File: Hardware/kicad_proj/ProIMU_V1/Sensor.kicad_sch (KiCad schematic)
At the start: 5 parts

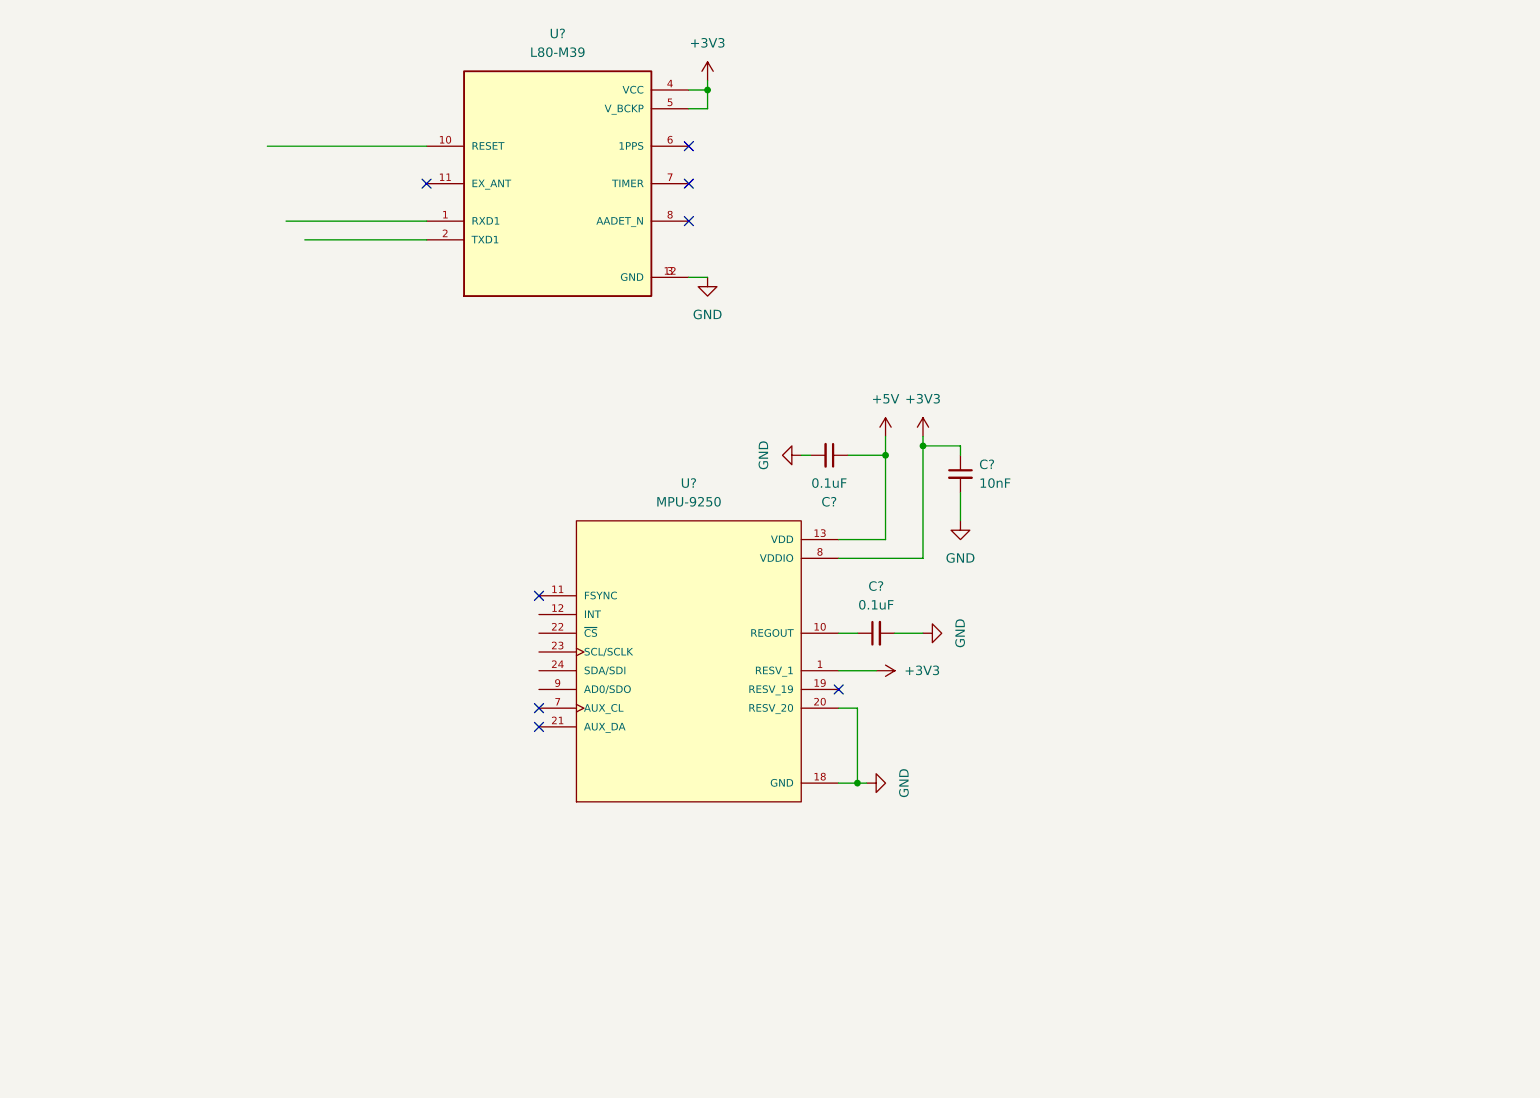
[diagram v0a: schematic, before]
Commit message: Added sensor schematic
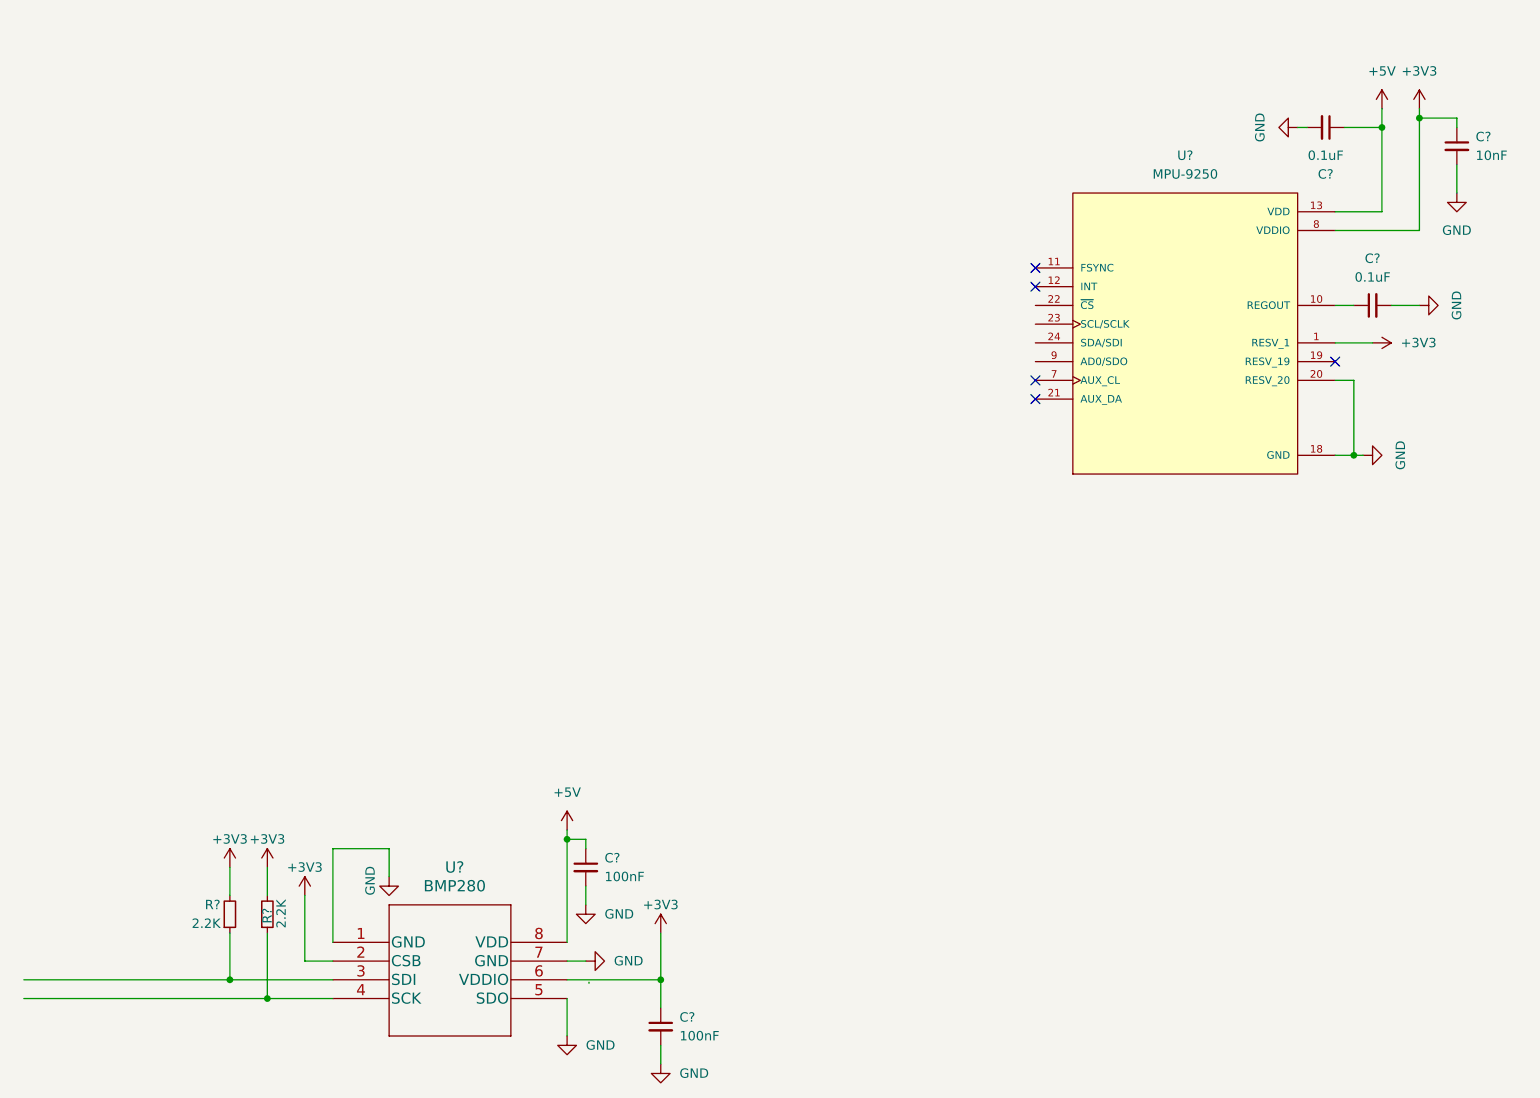
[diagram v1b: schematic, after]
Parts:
- removed C?: 10nF, Capacitor_SMD:C_0402_1005Metric_Pad0.74x0.62mm_HandSolder, symbol Device:C_Small
- removed C? (x2): 0.1uF, Capacitor_SMD:C_0402_1005Metric_Pad0.74x0.62mm_HandSolder, symbol Device:C_Small
- removed U?: L80-M39, footprints:XCVR_L80-M39, symbol L80-M39:L80-M39
- removed U?: MPU-9250, QFN40P300X300X105-24N, symbol MPU-9250:MPU-9250
- added C? (x2): 0.1uF, Capacitor_SMD:C_0402_1005Metric_Pad0.74x0.62mm_HandSolder, symbol Device:C_Small
- added C? (x2): 100nF, Capacitor_SMD:C_0402_1005Metric_Pad0.74x0.62mm_HandSolder, symbol Device:C_Small
- added C?: 10nF, Capacitor_SMD:C_0402_1005Metric_Pad0.74x0.62mm_HandSolder, symbol Device:C_Small
- added R? (x2): 2.2K, Resistor_SMD:R_0402_1005Metric_Pad0.72x0.64mm_HandSolder, symbol Device:R_Small
- added U?: MPU-9250, QFN40P300X300X105-24N, symbol MPU-9250:MPU-9250
- added U?: BMP280, footprints:BMP280, symbol 2022-02-05_19-44-07:BMP280
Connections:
- net +3V3: now also C?.1, C?.1, R?.2, R?.2, U?.1 (RESV_1), U?.2 (CSB), U?.6 (VDDIO), U?.8 (VDDIO)
- net +5V: now also C?.1, C?.1, U?.13 (VDD), U?.8 (VDD)
- net GND: now also C?.2, C?.2, C?.2, C?.2, C?.2, U?.1 (GND), U?.18 (GND), U?.20 (RESV_20), U?.5 (SDO), U?.7 (GND)
- new net: R?.1, U?.4 (SCK)
- new net: C?.1, U?.10 (REGOUT)
- new net: R?.1, U?.3 (SDI)
- no-connect marks 8 -> 5

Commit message: Updated schematic and removed redundant schematic
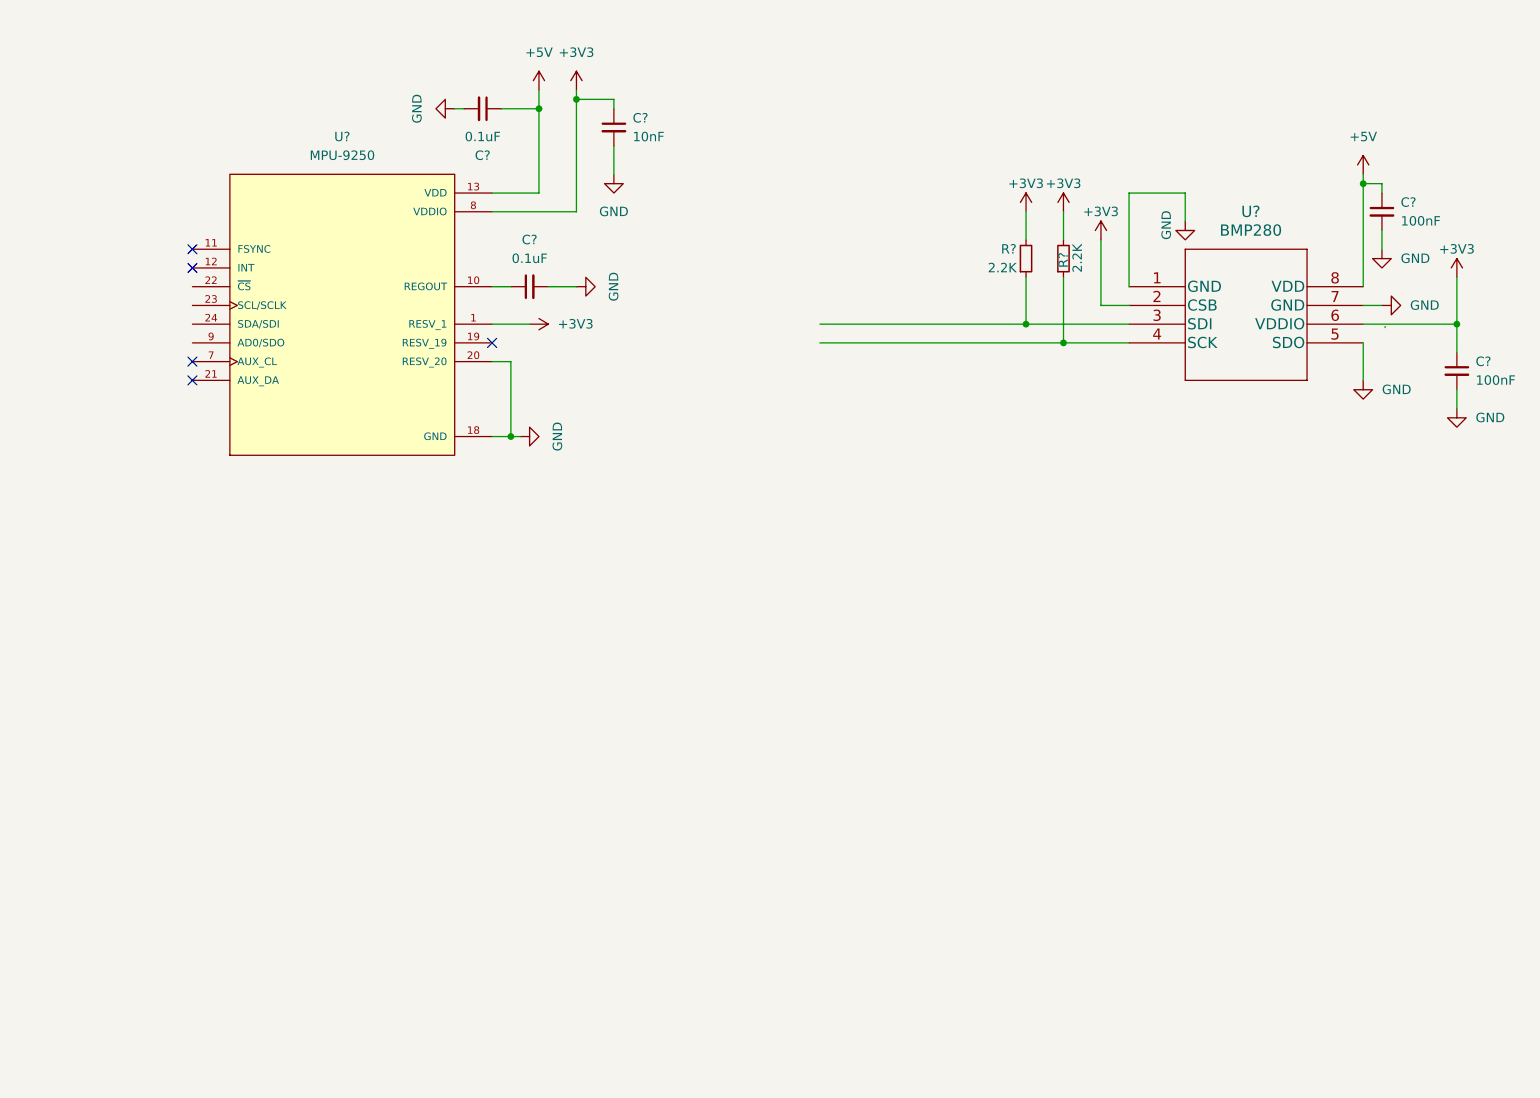
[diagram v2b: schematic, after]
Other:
- moved on the sheet: C?, R?, U?

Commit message: Updated Schematic and Layout
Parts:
- gave numbers to parts that had none: 9
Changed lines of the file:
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@@
   (symbol (lib_id "Device:C_Small") (at 99.06 39.37 270) (unit 1)
     (in_bom yes) (on_board yes) (fields_autoplaced)
-    (property "Reference" "C?" (id 0) (at 99.0537 45.72 90))
+    (property "Reference" "C9" (id 0) (at 99.0537 45.72 90))
     (property "Value" "0.1uF" (id 1) (at 99.0537 43.18 90))
     (property "Footprint" "Capacitor_SMD:C_0402_1005Metric_Pad0.74x0.62mm_HandSolder" (id 2) (at 99.06 39.37 0)
@@
   (symbol (lib_id "power:GND") (at 231.14 80.01 0) (unit 1)
     (in_bom yes) (on_board yes) (fields_autoplaced)
-    (property "Reference" "#PWR?" (id 0) (at 231.14 86.36 0)
+    (property "Reference" "#PWR0139" (id 0) (at 231.14 86.36 0)
       (effects (font (size 1.27 1.27)) hide)
     )
@@
   (symbol (lib_id "power:GND") (at 194.31 54.61 0) (unit 1)
     (in_bom yes) (on_board yes)
-    (property "Reference" "#PWR?" (id 0) (at 194.31 60.96 0)
+    (property "Reference" "#PWR0138" (id 0) (at 194.31 60.96 0)
       (effects (font (size 1.27 1.27)) hide)
     )
@@
   (symbol (lib_id "power:GND") (at 220.98 58.42 0) (unit 1)
     (in_bom yes) (on_board yes) (fields_autoplaced)
-    (property "Reference" "#PWR?" (id 0) (at 220.98 64.77 0)
+    (property "Reference" "#PWR0137" (id 0) (at 220.98 64.77 0)
       (effects (font (size 1.27 1.27)) hide)
     )
@@
   (symbol (lib_id "power:+3V3") (at 182.88 57.15 0) (unit 1)
     (in_bom yes) (on_board yes)
-    (property "Reference" "#PWR?" (id 0) (at 182.88 60.96 0)
+    (property "Reference" "#PWR0134" (id 0) (at 182.88 60.96 0)
       (effects (font (size 1.27 1.27)) hide)
     )
@@
   (symbol (lib_id "power:+3V3") (at 231.14 62.23 0) (unit 1)
     (in_bom yes) (on_board yes)
-    (property "Reference" "#PWR?" (id 0) (at 231.14 66.04 0)
+    (property "Reference" "#PWR0135" (id 0) (at 231.14 66.04 0)
       (effects (font (size 1.27 1.27)) hide)
     )
@@
   (symbol (lib_id "power:GND") (at 220.98 66.04 90) (unit 1)
     (in_bom yes) (on_board yes) (fields_autoplaced)
-    (property "Reference" "#PWR?" (id 0) (at 227.33 66.04 0)
+    (property "Reference" "#PWR0136" (id 0) (at 227.33 66.04 0)
       (effects (font (size 1.27 1.27)) hide)
     )
@@
   (symbol (lib_id "Device:R_Small") (at 177.8 59.69 0) (mirror x) (unit 1)
     (in_bom yes) (on_board yes)
-    (property "Reference" "R?" (id 0) (at 177.8 60.96 90)
+    (property "Reference" "R14" (id 0) (at 177.8 60.96 90)
       (effects (font (size 1.27 1.27)) (justify right))
     )
@@
   (symbol (lib_id "power:+3V3") (at 111.76 36.83 0) (unit 1)
     (in_bom yes) (on_board yes) (fields_autoplaced)
-    (property "Reference" "#PWR?" (id 0) (at 111.76 40.64 0)
+    (property "Reference" "#PWR0131" (id 0) (at 111.76 40.64 0)
       (effects (font (size 1.27 1.27)) hide)
     )
@@
   (symbol (lib_id "Device:C_Small") (at 231.14 74.93 0) (unit 1)
     (in_bom yes) (on_board yes) (fields_autoplaced)
-    (property "Reference" "C?" (id 0) (at 233.68 73.6662 0)
+    (property "Reference" "C13" (id 0) (at 233.68 73.6662 0)
       (effects (font (size 1.27 1.27)) (justify left))
     )
@@
   (symbol (lib_id "Device:C_Small") (at 105.41 63.5 90) (unit 1)
     (in_bom yes) (on_board yes) (fields_autoplaced)
-    (property "Reference" "C?" (id 0) (at 105.4163 57.15 90))
+    (property "Reference" "C10" (id 0) (at 105.4163 57.15 90))
     (property "Value" "0.1uF" (id 1) (at 105.4163 59.69 90))
     (property "Footprint" "Capacitor_SMD:C_0402_1005Metric_Pad0.74x0.62mm_HandSolder" (id 2) (at 105.41 63.5 0)
@@
   (symbol (lib_name "MPU-9250_1") (lib_id "MPU-9250:MPU-9250") (at 80.01 68.58 0) (unit 1)
     (in_bom yes) (on_board yes) (fields_autoplaced)
-    (property "Reference" "U?" (id 0) (at 80.01 43.18 0))
+    (property "Reference" "U5" (id 0) (at 80.01 43.18 0))
     (property "Value" "MPU-9250" (id 1) (at 80.01 45.72 0))
     (property "Footprint" "QFN40P300X300X105-24N" (id 2) (at 80.01 68.58 0)
@@
   (symbol (lib_id "Device:C_Small") (at 116.84 41.91 0) (unit 1)
     (in_bom yes) (on_board yes) (fields_autoplaced)
-    (property "Reference" "C?" (id 0) (at 119.38 40.6462 0)
+    (property "Reference" "C11" (id 0) (at 119.38 40.6462 0)
       (effects (font (size 1.27 1.27)) (justify left))
     )
@@
   (symbol (lib_id "power:+3V3") (at 105.41 68.58 270) (unit 1)
     (in_bom yes) (on_board yes) (fields_autoplaced)
-    (property "Reference" "#PWR?" (id 0) (at 101.6 68.58 0)
+    (property "Reference" "#PWR0128" (id 0) (at 101.6 68.58 0)
       (effects (font (size 1.27 1.27)) hide)
     )
@@
   (symbol (lib_id "power:GND") (at 95.25 39.37 270) (unit 1)
     (in_bom yes) (on_board yes) (fields_autoplaced)
-    (property "Reference" "#PWR?" (id 0) (at 88.9 39.37 0)
+    (property "Reference" "#PWR0125" (id 0) (at 88.9 39.37 0)
       (effects (font (size 1.27 1.27)) hide)
     )
@@
   (symbol (lib_id "power:+3V3") (at 177.8 53.34 0) (unit 1)
     (in_bom yes) (on_board yes)
-    (property "Reference" "#PWR?" (id 0) (at 177.8 57.15 0)
+    (property "Reference" "#PWR0133" (id 0) (at 177.8 57.15 0)
       (effects (font (size 1.27 1.27)) hide)
     )
@@
   (symbol (lib_id "power:+5V") (at 218.44 48.26 0) (unit 1)
     (in_bom yes) (on_board yes) (fields_autoplaced)
-    (property "Reference" "#PWR?" (id 0) (at 218.44 52.07 0)
+    (property "Reference" "#PWR0141" (id 0) (at 218.44 52.07 0)
       (effects (font (size 1.27 1.27)) hide)
     )
@@
   (symbol (lib_id "power:GND") (at 111.76 63.5 90) (unit 1)
     (in_bom yes) (on_board yes) (fields_autoplaced)
-    (property "Reference" "#PWR?" (id 0) (at 118.11 63.5 0)
+    (property "Reference" "#PWR0130" (id 0) (at 118.11 63.5 0)
       (effects (font (size 1.27 1.27)) hide)
     )
@@
   (symbol (lib_id "2022-02-05_19-44-07:BMP280") (at 186.69 63.5 0) (unit 1)
     (in_bom yes) (on_board yes) (fields_autoplaced)
-    (property "Reference" "U?" (id 0) (at 203.2 53.34 0)
+    (property "Reference" "U6" (id 0) (at 203.2 53.34 0)
       (effects (font (size 1.524 1.524)))
     )
@@
   (symbol (lib_id "power:+5V") (at 106.68 36.83 0) (unit 1)
     (in_bom yes) (on_board yes) (fields_autoplaced)
-    (property "Reference" "#PWR?" (id 0) (at 106.68 40.64 0)
+    (property "Reference" "#PWR0126" (id 0) (at 106.68 40.64 0)
       (effects (font (size 1.27 1.27)) hide)
     )
@@
   (symbol (lib_id "power:+3V3") (at 172.72 53.34 0) (unit 1)
     (in_bom yes) (on_board yes)
-    (property "Reference" "#PWR?" (id 0) (at 172.72 57.15 0)
+    (property "Reference" "#PWR0132" (id 0) (at 172.72 57.15 0)
       (effects (font (size 1.27 1.27)) hide)
     )
@@
   (symbol (lib_id "Device:R_Small") (at 172.72 59.69 0) (mirror x) (unit 1)
     (in_bom yes) (on_board yes)
-    (property "Reference" "R?" (id 0) (at 171.45 58.42 0)
+    (property "Reference" "R13" (id 0) (at 171.45 58.42 0)
       (effects (font (size 1.27 1.27)) (justify right))
     )
@@
   (symbol (lib_id "power:GND") (at 116.84 48.26 0) (unit 1)
     (in_bom yes) (on_board yes) (fields_autoplaced)
-    (property "Reference" "#PWR?" (id 0) (at 116.84 54.61 0)
+    (property "Reference" "#PWR0127" (id 0) (at 116.84 54.61 0)
       (effects (font (size 1.27 1.27)) hide)
     )
@@
   (symbol (lib_id "power:GND") (at 104.14 83.82 90) (unit 1)
     (in_bom yes) (on_board yes) (fields_autoplaced)
-    (property "Reference" "#PWR?" (id 0) (at 110.49 83.82 0)
+    (property "Reference" "#PWR0129" (id 0) (at 110.49 83.82 0)
       (effects (font (size 1.27 1.27)) hide)
     )
@@
   (symbol (lib_id "Device:C_Small") (at 220.98 53.34 0) (unit 1)
     (in_bom yes) (on_board yes) (fields_autoplaced)
-    (property "Reference" "C?" (id 0) (at 223.52 52.0762 0)
+    (property "Reference" "C12" (id 0) (at 223.52 52.0762 0)
       (effects (font (size 1.27 1.27)) (justify left))
     )
@@
   (symbol (lib_id "power:GND") (at 218.44 76.2 0) (unit 1)
     (in_bom yes) (on_board yes) (fields_autoplaced)
-    (property "Reference" "#PWR?" (id 0) (at 218.44 82.55 0)
-      (effects (font (size 1.27 1.27)) hide)
-    )
+    (property "Reference" "#PWR0140" (id 0) (at 218.44 82.55 0)
+      (effects (font (size 1.27 1.27)) hide)
+    )

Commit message: Updated Repo
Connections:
- net +3V3: now also U5.22 (~{CS})
- net SENSOR_I2C1_SCL: now reaches U6.4 (SCK)
- net SENSOR_I2C1_SCL: now also R13.1, U5.23 (SCL/SCLK); no longer R14.1
- net SENSOR_I2C1_SDA: now reaches U5.24 (SDA/SDI)
- net SENSOR_I2C1_SDA: now also R14.1, U6.3 (SDI)
- no-connect marks 5 -> 6
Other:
- moved on the sheet: C10, C11, C12, C13, C9, R13, U5, U6
